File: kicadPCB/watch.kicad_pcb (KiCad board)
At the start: 2 copper layers, 81 x 53 mm, 64 parts, among them IC1 ISL1209, J2 USB-MICROB, M1 BOS_LIBS_SWD_BREAKOUTS, T1 BC850, U2 MKL27Z256VLH4, Y1 Crystal

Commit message: added laser warning text
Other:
- board text added: "LASER RADIATION DO NOT STARE INTO BEAM"
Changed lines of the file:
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@@
     (area 107.917149 78.430582 189.085051 131.576618)
     (thickness 1.6)
-    (drawings 85)
+    (drawings 86)
     (tracks 800)
     (zones 0)
@@
       (net 60 /PTA3))
   )
+  (gr_text "LASER RADIATION\nDO NOT STARE INTO BEAM" (at 112.268 82.55 270) (layer F.SilkS)
+    (effects (font (size 0.3 0.3) (thickness 0.075)))
+  )
   (gr_line (start 107.99215 131.501617) (end 127.294219 131.501617) (layer Edge.Cuts) (width 0.15))

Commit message: added clearer labels
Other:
- board text added: "IR LED"
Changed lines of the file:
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@@
     (area 107.917149 78.430582 189.085051 131.576618)
     (thickness 1.6)
-    (drawings 86)
+    (drawings 87)
     (tracks 800)
     (zones 0)
@@
       (net 60 /PTA3))
   )
+  (gr_text "IR LED" (at 137.16 80.772) (layer F.SilkS)
+    (effects (font (size 0.5 0.5) (thickness 0.125)))
+  )
   (gr_text "LASER RADIATION\nDO NOT STARE INTO BEAM" (at 112.268 82.55 270) (layer F.SilkS)

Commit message: fixed spi1
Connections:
- U$4 pad DS: /PTB19 -> /PTB16
- U$4 pad SHCP: /PTC0 -> /PTC3
- U$5 pad SHCP: /PTC0 -> /PTC3
- U2 pad 46: Net-(U2-Pad46) -> /PTC3
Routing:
- net /PTC3: track 0.00 -> 64.2 mm, vias 0 -> 2
- net /PTC0: track 58.5 -> 0.00 mm, vias 2 -> 0
- net /PTB16: track 0.00 -> 8.90 mm, vias 0 -> 1
- net /PTB19: track 6.59 -> 0.00 mm, vias 1 -> 0

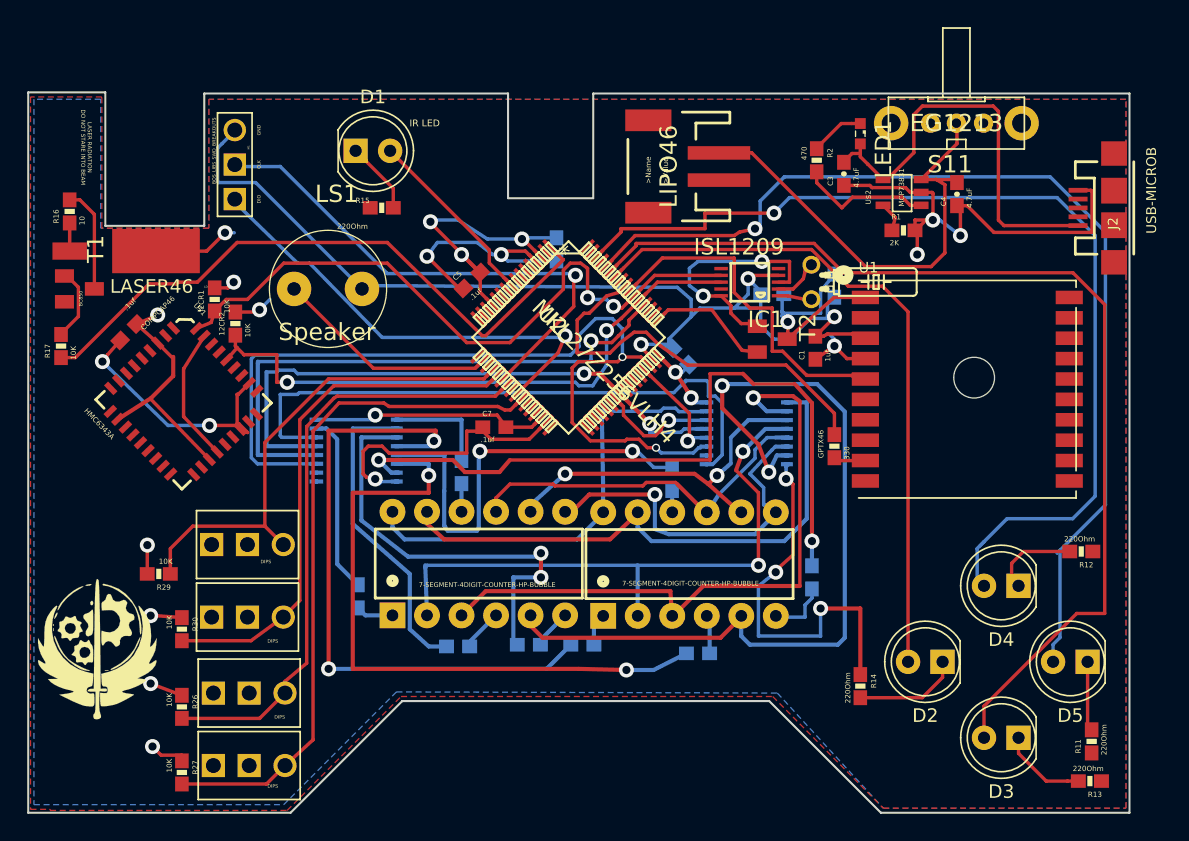
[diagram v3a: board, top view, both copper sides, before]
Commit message: fixed uart gps
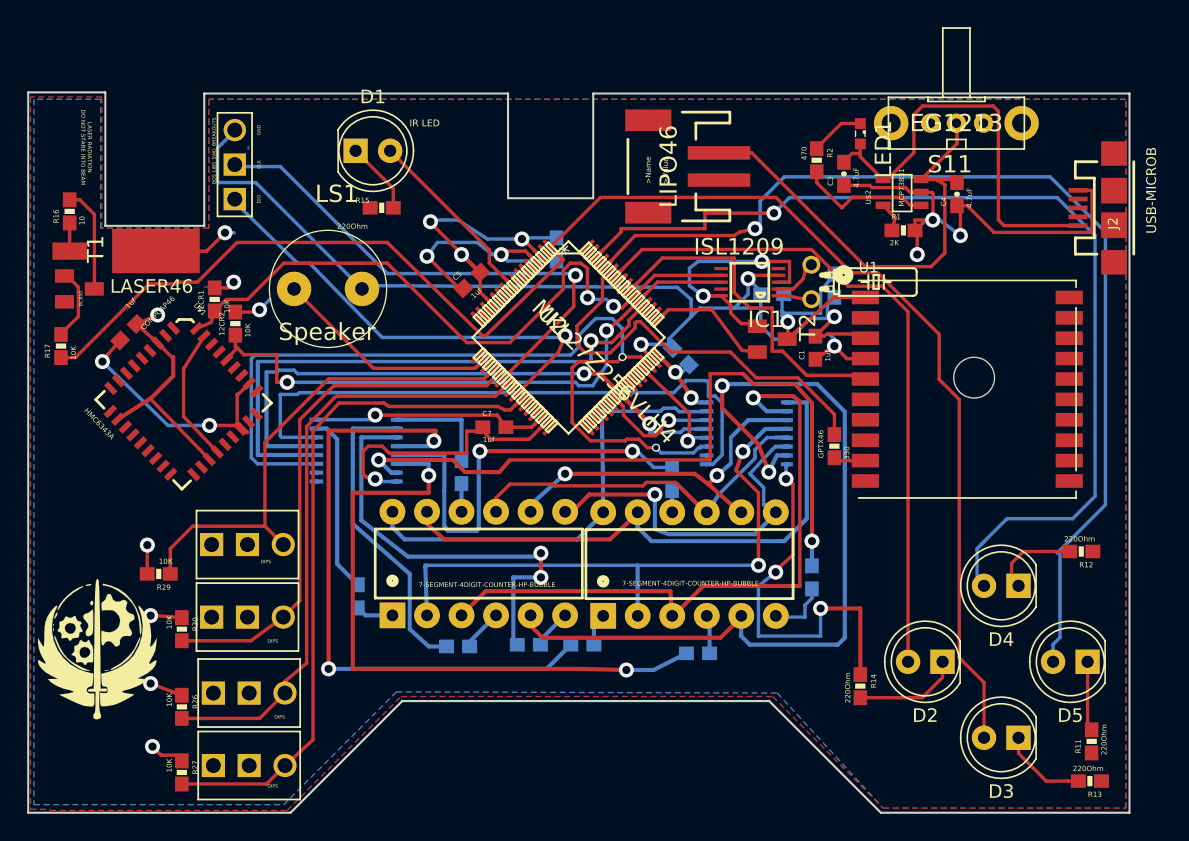
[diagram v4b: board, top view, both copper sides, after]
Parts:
- R10, R3, R4, R5, R6, R7, R8, R9: value 680 -> 330
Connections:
- D3 pad 2: /PTD2 -> /PTE0
- GPTX46 pad 2: /PTC11 -> /PTD2
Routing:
- net /PTE0: track 46.9 -> 112.2 mm
- net /PTD2: track 76.6 -> 32.4 mm
- net /PTC11: track 30.3 -> 0.71 mm
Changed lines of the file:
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@@
     (thickness 1.6)
     (drawings 87)
-    (tracks 817)
+    (tracks 820)
     (zones 0)
     (modules 64)
@@
       (effects (font (size 0.38608 0.38608) (thickness 0.032512)) (justify left bottom mirror))
     )
-    (fp_text value 680 (at -1.016 -1.143 90) (layer B.SilkS)
+    (fp_text value 330 (at -1.016 -1.143 90) (layer B.SilkS)
       (effects (font (size 0.38608 0.38608) (thickness 0.032512)) (justify left bottom mirror))
     )
@@
       (effects (font (size 0.38608 0.38608) (thickness 0.032512)) (justify left bottom mirror))
     )
-    (fp_text value 680 (at -1.016 -1.143 90) (layer B.SilkS)
+    (fp_text value 330 (at -1.016 -1.143 90) (layer B.SilkS)
       (effects (font (size 0.38608 0.38608) (thickness 0.032512)) (justify left bottom mirror))
     )
@@
       (effects (font (size 0.38608 0.38608) (thickness 0.032512)) (justify left bottom mirror))
     )
-    (fp_text value 680 (at -1.016 -1.143 180) (layer B.SilkS)
+    (fp_text value 330 (at -1.016 -1.143 180) (layer B.SilkS)
       (effects (font (size 0.38608 0.38608) (thickness 0.032512)) (justify left bottom mirror))
     )
@@
       (effects (font (size 0.38608 0.38608) (thickness 0.032512)) (justify left bottom mirror))
     )
-    (fp_text value 680 (at -1.016 -1.143 90) (layer B.SilkS)
+    (fp_text value 330 (at -1.016 -1.143 90) (layer B.SilkS)
       (effects (font (size 0.38608 0.38608) (thickness 0.032512)) (justify left bottom mirror))
     )
@@
       (effects (font (size 0.38608 0.38608) (thickness 0.032512)) (justify left bottom mirror))
     )
-    (fp_text value 680 (at -1.016 -1.143 180) (layer B.SilkS)
+    (fp_text value 330 (at -1.016 -1.143 180) (layer B.SilkS)
       (effects (font (size 0.38608 0.38608) (thickness 0.032512)) (justify left bottom mirror))
     )
@@
       (effects (font (size 0.38608 0.38608) (thickness 0.032512)) (justify left bottom mirror))
     )
-    (fp_text value 680 (at -1.016 -1.143 180) (layer B.SilkS)
+    (fp_text value 330 (at -1.016 -1.143 180) (layer B.SilkS)
       (effects (font (size 0.38608 0.38608) (thickness 0.032512)) (justify left bottom mirror))
     )
@@
       (effects (font (size 0.38608 0.38608) (thickness 0.032512)) (justify left bottom mirror))
     )
-    (fp_text value 680 (at -1.016 -1.143 90) (layer B.SilkS)
+    (fp_text value 330 (at -1.016 -1.143 90) (layer B.SilkS)
       (effects (font (size 0.38608 0.38608) (thickness 0.032512)) (justify left bottom mirror))
     )
@@
       (effects (font (size 0.38608 0.38608) (thickness 0.032512)) (justify left bottom mirror))
     )
-    (fp_text value 680 (at -1.016 -1.143 180) (layer B.SilkS)
+    (fp_text value 330 (at -1.016 -1.143 180) (layer B.SilkS)
       (effects (font (size 0.38608 0.38608) (thickness 0.032512)) (justify left bottom mirror))
     )
@@
       (net 23 /N$30))
     (pad 2 smd rect (at 0.85 0 90) (size 1.1 1) (layers Top F.Paste F.Mask)
-      (net 24 /PTC11))
+      (net 118 /PTD2))
   )
   (module 0603 (layer Bottom)
@@
       (net 49 /N$38))
     (pad 2 thru_hole circle (at 2.54 0 180) (size 1.8 1.8) (drill 0.9) (layers *.Cu *.Mask)
-      (net 118 /PTD2))
+      (net 53 /PTE0))
     (model LEDs.3dshapes/LED_D5.0mm.wrl
       (at (xyz 0 0 0))
@@
   (segment (start 169.581244 105.593589) (end 167.302244 105.593589) (width 0.254) (layer Top) (net 23))
   (segment (start 167.302244 105.593589) (end 167.302244 105.384589) (width 0.254) (layer Top) (net 23))
-  (segment (start 167.302244 102.121589) (end 163.746244 98.565589) (width 0.254) (layer Top) (net 24))
-  (segment (start 163.746244 98.565589) (end 156.507244 98.565589) (width 0.254) (layer Top) (net 24))
-  (segment (start 156.507244 98.565589) (end 154.348244 97.041589) (width 0.254) (layer Top) (net 24))
-  (segment (start 150.792244 97.676589) (end 148.379244 97.676589) (width 0.254) (layer Top) (net 24))
-  (segment (start 148.379244 97.676589) (end 148.379244 95.263589) (width 0.254) (layer Top) (net 24))
-  (segment (start 152.570244 96.152589) (end 153.459244 96.152589) (width 0.254) (layer Top) (net 24))
-  (segment (start 153.459244 96.152589) (end 154.348244 97.041589) (width 0.254) (layer Top) (net 24))
-  (segment (start 167.302244 103.684589) (end 167.302244 102.121589) (width 0.254) (layer Top) (net 24))
-  (segment (start 150.792244 97.676589) (end 151.554244 96.914589) (width 0.254) (layer Top) (net 24))
-  (segment (start 151.554244 96.914589) (end 152.570244 96.152589) (width 0.254) (layer Top) (net 24))
-  (segment (start 148.379244 95.263589) (end 148.887244 94.755589) (width 0.254) (layer Top) (net 24))
-  (segment (start 148.887244 94.755589) (end 149.268244 94.755589) (width 0.254) (layer Top) (net 24))
-  (segment (start 149.268244 94.755589) (end 150.538244 93.485589) (width 0.254) (layer Top) (net 24))
   (segment (start 151.399782 93.231589) (end 151.898491 92.73288) (width 0.254) (layer Top) (net 24))
-  (segment (start 150.538244 93.485589) (end 151.399782 93.231589) (width 0.254) (layer Top) (net 24))
   (segment (start 158.966144 91.969589) (end 154.076025 91.969589) (width 0.254) (layer Top) (net 25))
   (segment (start 154.076025 91.969589) (end 152.605613 93.440001) (width 0.254) (layer Top) (net 25))
@@
   (segment (start 112.86 87.481345) (end 111.791244 86.412589) (width 0.25) (layer Top) (net 52))
   (segment (start 111.791244 86.412589) (end 111.041244 86.412589) (width 0.25) (layer Top) (net 52))
+  (segment (start 178.308 125.984) (end 178.308 121.921835) (width 0.25) (layer Top) (net 53))
+  (segment (start 150.087285 86.235588) (end 146.587912 89.734961) (width 0.25) (layer Top) (net 53))
+  (segment (start 178.308 121.921835) (end 176.485001 120.098836) (width 0.25) (layer Top) (net 53))
+  (segment (start 176.485001 101.098348) (end 175.006 99.619347) (width 0.25) (layer Top) (net 53))
+  (segment (start 170.487666 91.778599) (end 168.547176 91.778599) (width 0.25) (layer Top) (net 53))
+  (segment (start 163.004165 86.235588) (end 150.087285 86.235588) (width 0.25) (layer Top) (net 53))
+  (segment (start 176.485001 120.098836) (end 176.485001 101.098348) (width 0.25) (layer Top) (net 53))
+  (segment (start 175.006 99.619347) (end 175.006 96.296933) (width 0.25) (layer Top) (net 53))
+  (segment (start 146.587912 89.734961) (end 146.418419 89.904454) (width 0.25) (layer Top) (net 53))
+  (segment (start 175.006 96.296933) (end 170.487666 91.778599) (width 0.25) (layer Top) (net 53))
+  (segment (start 168.547176 91.778599) (end 163.004165 86.235588) (width 0.25) (layer Top) (net 53))
   (segment (start 134.409244 89.548589) (end 141.394244 96.406589) (width 0.254) (layer Top) (net 53))
   (segment (start 141.394244 96.406589) (end 141.648244 96.406589) (width 0.254) (layer Top) (net 53))
@@
   (segment (start 151.191385 91.943448) (end 151.191385 92.02577) (width 0.254) (layer Top) (net 117))
   (segment (start 172.636244 120.367195) (end 172.890244 119.774589) (width 0.254) (layer Bottom) (net 117))
-  (segment (start 187.188245 116.84) (end 187.188245 94.115588) (width 0.25) (layer Top) (net 118))
-  (segment (start 185.130998 116.84) (end 187.188245 116.84) (width 0.25) (layer Top) (net 118))
-  (segment (start 178.308 125.984) (end 178.308 123.662998) (width 0.25) (layer Top) (net 118))
-  (segment (start 178.308 123.662998) (end 185.130998 116.84) (width 0.25) (layer Top) (net 118))
-  (segment (start 152.713154 89.616578) (end 152.713154 89.782441) (width 0.25) (layer Top) (net 118))
-  (segment (start 187.188245 94.115588) (end 184.851255 91.778598) (width 0.25) (layer Top) (net 118))
-  (segment (start 184.851255 91.778598) (end 167.967663 91.778598) (width 0.25) (layer Top) (net 118))
-  (segment (start 167.967663 91.778598) (end 165.805643 89.616578) (width 0.25) (layer Top) (net 118))
-  (segment (start 165.805643 89.616578) (end 152.713154 89.616578) (width 0.25) (layer Top) (net 118))
-  (segment (start 152.713154 89.782441) (end 151.055595 91.44) (width 0.25) (layer Top) (net 118))
+  (segment (start 167.302244 103.684589) (end 167.302244 102.194665) (width 0.25) (layer Top) (net 118))
+  (segment (start 167.302244 102.194665) (end 164.618158 99.510579) (width 0.25) (layer Top) (net 118))
+  (segment (start 148.973323 97.66659) (end 148.369245 97.062512) (width 0.25) (layer Top) (net 118))
+  (segment (start 164.618158 99.510579) (end 161.556392 99.510579) (width 0.25) (layer Top) (net 118))
+  (segment (start 152.641254 95.457811) (end 152.641254 95.840025) (width 0.25) (layer Top) (net 118))
+  (segment (start 161.556392 99.510579) (end 159.656111 97.610298) (width 0.25) (layer Top) (net 118))
+  (segment (start 152.722065 95.377) (end 152.641254 95.457811) (width 0.25) (layer Top) (net 118))
+  (segment (start 152.641254 95.840025) (end 150.814689 97.66659) (width 0.25) (layer Top) (net 118))
+  (segment (start 150.814689 97.66659) (end 148.973323 97.66659) (width 0.25) (layer Top) (net 118))
+  (segment (start 150.241 93.813755) (end 150.241 92.219149) (width 0.25) (layer Top) (net 118))
+  (segment (start 159.656111 97.610298) (end 155.274567 97.610298) (width 0.25) (layer Top) (net 118))
+  (segment (start 155.274567 97.610298) (end 153.041269 95.377) (width 0.25) (layer Top) (net 118))
+  (segment (start 153.041269 95.377) (end 152.722065 95.377) (width 0.25) (layer Top) (net 118))
+  (segment (start 148.369245 97.062512) (end 148.369245 95.68551) (width 0.25) (layer Top) (net 118))
+  (segment (start 148.369245 95.68551) (end 150.241 93.813755) (width 0.25) (layer Top) (net 118))
+  (segment (start 150.241 92.219149) (end 151.020149 91.44) (width 0.25) (layer Top) (net 118))
   (segment (start 151.055595 91.44) (end 151.020149 91.44) (width 0.25) (layer Top) (net 118))
   (segment (start 151.020149 91.44) (end 150.440075 92.020074) (width 0.25) (layer Top) (net 118))
